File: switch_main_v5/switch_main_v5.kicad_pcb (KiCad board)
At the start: 6 copper layers, 93 x 50 mm, 646 parts, among them J1201 MKXS1-1 Power Input, J301 MKXS1-1 Power Input, J3601 MSPE-J2L0-B00, J3602 JST-GH-2-Horizontal, J3603 MSPE-J2L0-B00, J3604 JST-GH-2-Horizontal, J3605 MSPE-J2L0-x00, J3606 MSPE-J2L0-x00, J3607 ARJM11D7-502-AB-EW2, J3608 MSPE-J2L0-x00, Q1401 DMP21D0UFB-7B, Q1801 DMN21D2UFB-7B, Q1802 DMN21D2UFB-7B, Q1803 DMN21D2UFB-7B, Q2001 DMP21D0UFB-7B, Q2002 DMN21D2UFB-7B, Q2101 DMP21D0UFB-7B, Q2102 DMN21D2UFB-7B, Q2201 DMP21D0UFB-7B, Q2202 DMN21D2UFB-7B, Q2301 DMP21D0UFB-7B, Q2302 DMN21D2UFB-7B, Q2401 DMP21D0UFB-7B, Q2402 DMN21D2UFB-7B, Q3001 DMP21D0UFB-7B, Q3002 DMP21D0UFB-7B, Q3003 DMP21D0UFB-7B, Q3004 DMP21D0UFB-7B, Q3005 DMN21D2UFB-7B, Q3006 DMN21D2UFB-7B, Q3101 DMP21D0UFB-7B, Q3102 DMN21D2UFB-7B, Q3601 DMN21D2UFB-7B, Q3602 DMN21D2UFB-7B, Q3801 DMN21D2UFB-7B, Q3802 DMN21D2UFB-7B, T2701 74930100, T2801 74930100, T2901 74930100, T3301 74930100, T3401 74930100, T3501 74930100, U1001 TPS62290TDRVRQ1, U1101 TPS62290TDRVRQ1, U1201 TPS26600RHFR, U1202 TVS3301DRBR, U1301 MAX20075DATCA/V+, U1302 TPS7B8133QDRVRQ1, U1303 NCP508MT25TBG, U1401 STM32H573IIKxQ, U1402 FM25CL64B-DG, U1501 SJA1105QELY, U1601 SJA1105QELY, U1801 NX3L4051HRZ, U1802 LMK1C1104DQFR, U1803 LMK1C1104DQFR, U1901 DP83867IRRGZR, U2001 88Q2112-A2-NYD2A000-P123, U2101 88Q2112-A2-NYD2A000-P123, U2201 88Q2112-A2-NYD2A000-P123, U2301 88Q2112-A2-NYD2A000-P123, U2401 88Q2112-A2-NYD2A000-P123, U2501 LAN8671C2-E_U3B, U3001 TPS27S100BRRK, U3002 TPS27S100BRRK, U301 TPS26600RHFR, U302 TVS3301DRBR, U3101 NCS213RMUTAG, U3102 TPS27S100BRRK, U3701 ISO6521REUR, U3702 ISO6520REUR, U3801 STM32H503KBUx, U401 LMQ66430MC3RXBRQ1, U402 TPS2116DRL, U403 TPS7B8133QDRVRQ1, U501 TPS7A1409PDRVR, U502 TPS7A2025PDQNR, U601 TPS62290TDRVRQ1, U701 TPS62290TDRVRQ1, U801 TPS62290TDRVRQ1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

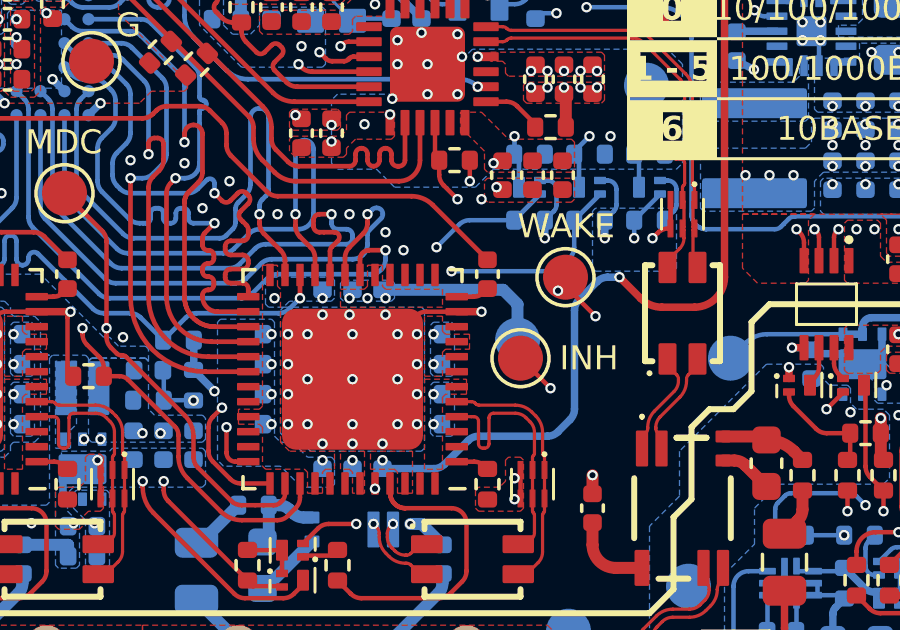
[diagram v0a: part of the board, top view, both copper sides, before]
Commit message: Updated crystal load capacitors
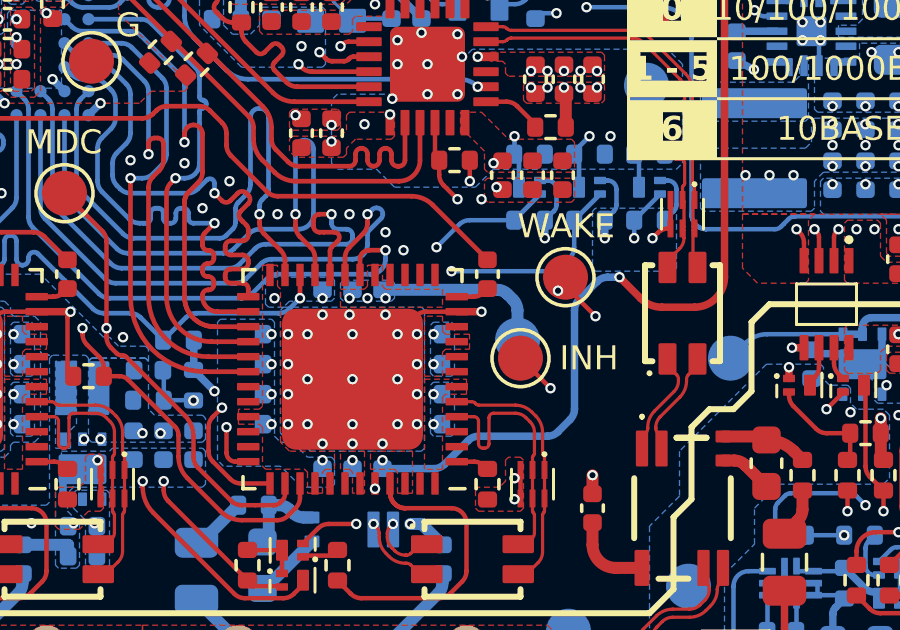
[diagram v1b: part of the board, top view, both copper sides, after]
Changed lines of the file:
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@@
 	)
 	(segment
-		(start 150.02 99.52)
-		(end 150.5 100)
+		(start 150.166447 99.666447)
+		(end 150.353554 99.853554)
 		(width 0.4)
 		(layer "B.Cu")
@@
 	(segment
 		(start 146 99.52)
-		(end 150.02 99.52)
+		(end 149.812893 99.52)
 		(width 0.4)
 		(layer "B.Cu")
@@
 	)
 	(segment
-		(start 150.5 100)
+		(start 150.5 100.207107)
 		(end 150.5 101.2)
 		(width 0.4)
@@
 		(net 109)
 	)
+	(arc
+		(start 150.5 100.207107)
+		(mid 150.46194 100.015766)
+		(end 150.353554 99.853554)
+		(width 0.4)
+		(layer "B.Cu")
+		(net 109)
+	)
+	(arc
+		(start 149.812893 99.52)
+		(mid 150.004235 99.55806)
+		(end 150.166447 99.666447)
+		(width 0.4)
+		(layer "B.Cu")
+		(net 109)
+	)
 	(via
 		(at 108.6 104.5)
@@
 			)
 		)
-	)
-	(zone
-		(net 109)
-		(net_name "+0V9_1")
-		(layer "B.Cu")
-		(name "$teardrop_padvia$")
-		(hatch none 0.1)
-		(priority 30007)
-		(attr
-			(teardrop
-				(type padvia)
-			)
-		)
-		(connect_pads yes
-			(clearance 0)
-		)
-		(min_thickness 0.0254)
-		(filled_areas_thickness no)
-		(fill yes
-			(thermal_gap 0.5)
-			(thermal_bridge_width 0.5)
-			(island_removal_mode 1)
-			(island_area_min 10)
-		)
-		(polygon
-			(pts
-				(xy 150.156637 99.93948) (xy 150.220339 100.029127) (xy 150.252423 100.137191) (xy 150.2532 100.265449)
-				(xy 150.220926 100.408808) (xy 150.166539 100.531188) (xy 150.153702 100.547245) (xy 150.500707 101.200707)
-				(xy 150.646964 100.464678) (xy 150.639716 100.444031) (xy 150.640549 100.370719) (xy 150.642243 100.22169)
-				(xy 150.62406 100.034999) (xy 150.600594 99.935969) (xy 150.563854 99.837648) (xy 150.511072 99.743412)
-				(xy 150.43948 99.656637)
-			)
-		)
